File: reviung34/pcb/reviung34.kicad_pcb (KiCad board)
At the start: 2 copper layers, 214.3 x 107.1 mm, 95 parts, among them SW1 SW_PUSH, SW10 SW_PUSH, SW11 SW_PUSH, SW12 SW_PUSH, SW13 SW_PUSH, SW14 SW_PUSH, SW15 SW_PUSH, SW16 SW_PUSH, SW17 SW_PUSH, SW18 SW_PUSH, SW19 SW_PUSH, SW2 SW_PUSH, SW20 SW_PUSH, SW21 SW_PUSH, SW22 SW_PUSH, SW23 SW_PUSH, SW24 SW_PUSH, SW25 SW_PUSH, SW26 SW_PUSH, SW27 SW_PUSH, SW28 SW_PUSH, SW29 SW_PUSH, SW3 SW_PUSH, SW30 SW_PUSH, SW31 SW_PUSH, SW32 SW_PUSH, SW33 SW_PUSH, SW34 SW_PUSH, SW35 SW_PUSH, SW4 SW_PUSH, SW5 SW_PUSH, SW6 SW_PUSH, SW7 SW_PUSH, SW8 SW_PUSH, SW9 SW_PUSH, U1 ProMicro

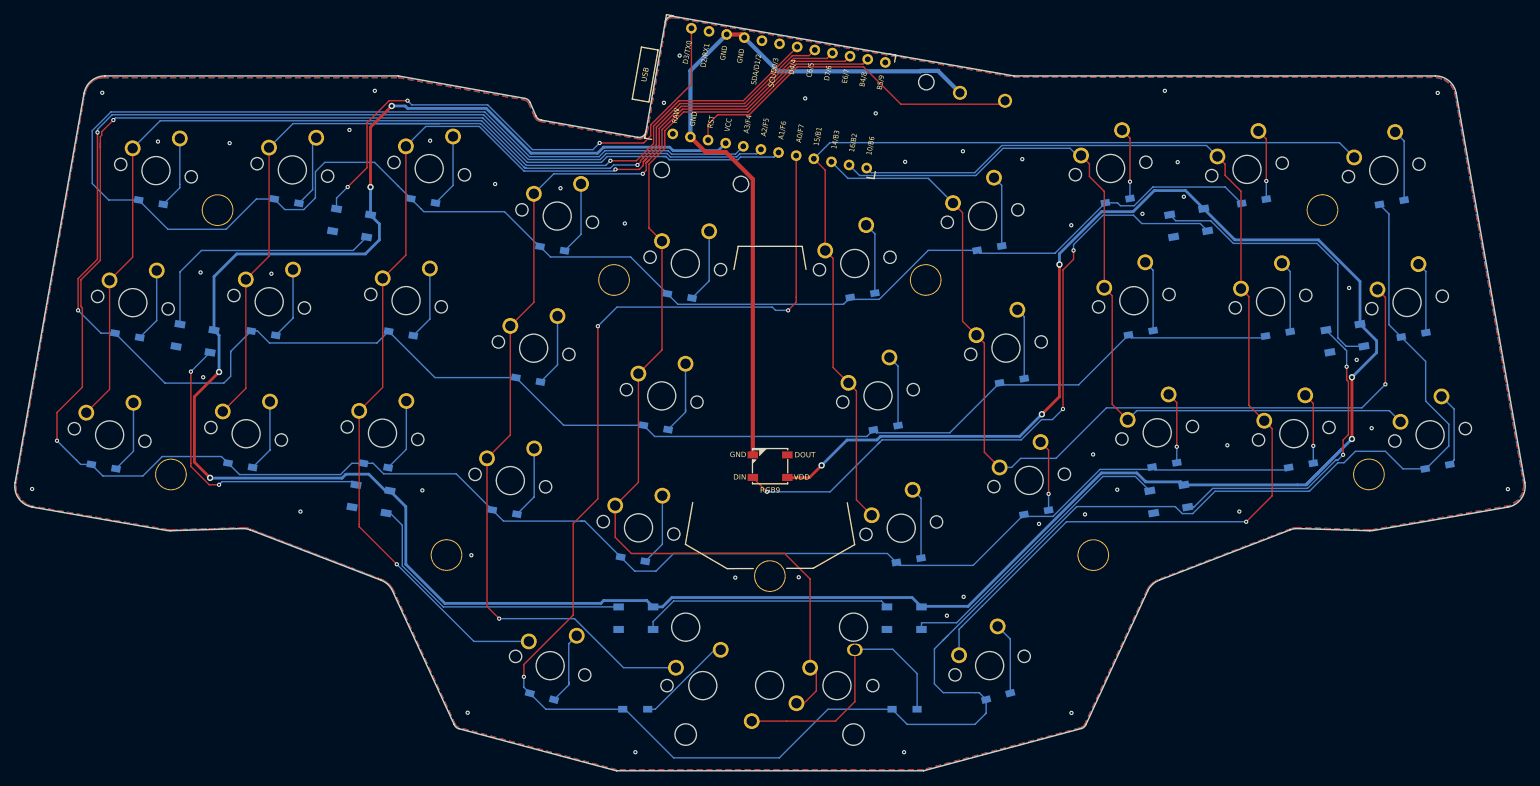
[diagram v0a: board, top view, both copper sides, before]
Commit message: choc version of r34
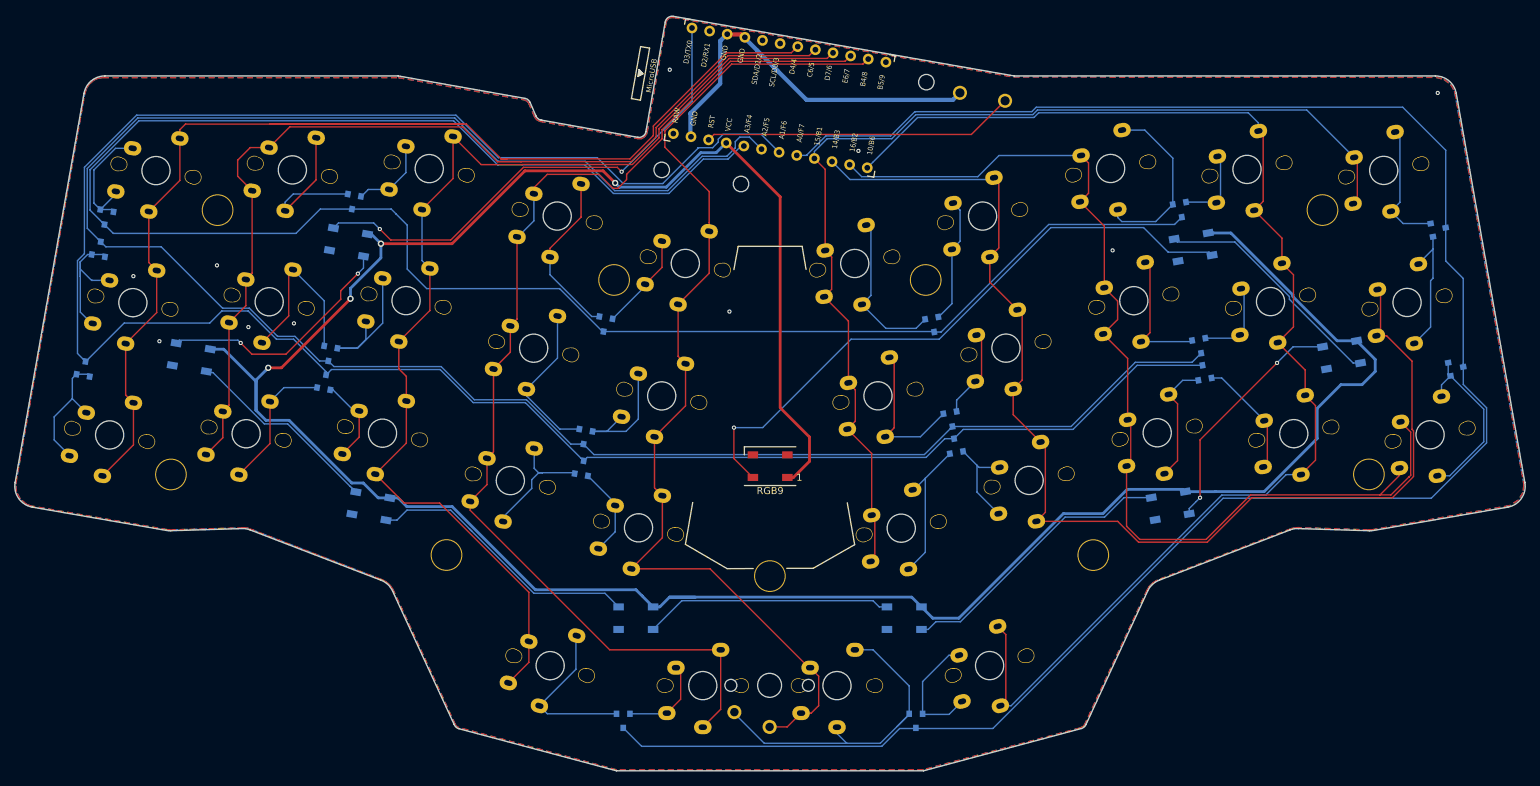
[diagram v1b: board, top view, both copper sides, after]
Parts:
- removed D12, D14, D17, D19, D2, D22, D23, D26, D27, D30, D32, D34, D4, D7, D9: 1N4148W, _reviung-kbd:D3_SMD_1side
- D1, D10, D11, D13, D15, D16, D18, D20, D21, D24, D25, D28, D29, D3, D31, D33, D5, D6, D8: value 1N4148W -> BAV70; footprint _reviung-kbd:D3_SMD_1side -> Package_TO_SOT_SMD:SOT-23
- RESET1: footprint _reviung-kbd:ResetSW_1side -> kbd-footprints:ResetSW_1side
- RGB1, RGB2, RGB3, RGB4, RGB5, RGB6, RGB7, RGB8, RGB9: footprint _reviung-kbd:LED_WS2812B_PLCC4_5.0x5.0mm_P3.2mm -> LED_SMD:LED_WS2812B_PLCC4_5.0x5.0mm_P3.2mm
- SW1, SW10, SW11, SW12, SW13, SW14, SW15, SW16, SW19, SW2, SW20, SW21, SW22, SW23, SW24, SW25, SW26, SW27, SW28, SW29, SW3, SW30, SW31, SW32, SW33, SW34, SW4, SW5, SW6, SW7, SW8, SW9: footprint _reviung-kbd:MXOnly-1U-NoLED -> kbd-footprints:CherryMX_Choc_1u
- SW17: footprint _reviung-kbd:MXOnly-1U-5pinRcut -> kbd-footprints:CherryMX_Choc_1u
- SW18: footprint _reviung-kbd:MXOnly-1U-5pinLcut -> kbd-footprints:CherryMX_Choc_1u
- SW35: footprint _reviung-kbd:MXOnly-2U-NoLED-or1Ux2 -> Keebio-Parts:Kailh-PG1350-1u-NoLED
- U1: footprint _reviung-kbd:ProMicro -> kbd-footprints:ProMicro_v3
- moved D28 14.9 mm to (164.2, 91.4), turned to 100 degrees
- moved D15 14.8 mm to (111.3, 94.6), turned to 80 degrees
- moved D29 14.3 mm to (199.5, 81.0), turned to 100 degrees
- moved D33 14.2 mm to (235.3, 80.4)
- moved D11 14.2 mm to (40.6, 80.5), turned to 80 degrees
- moved D13 13.9 mm to (74.8, 82.4), turned to 80 degrees
- moved D20 13.5 mm to (161.1, 74.3), turned to 280 degrees
- moved D6 12.9 mm to (42.8, 63.5), turned to 80 degrees
- moved D16 12.0 mm to (117.1, 130.5), turned to 270 degrees
- moved D5 11.4 mm to (114.5, 74.3), turned to 260 degrees
- moved D8 10.5 mm to (75.4, 78.5), turned to 260 degrees
- moved D24 10.2 mm to (163.6, 87.7), turned to 280 degrees
- moved D10 10.2 mm to (111.6, 90.2), turned to 260 degrees
- moved D3 9.93 mm to (78.8, 56.9), turned to 260 degrees
- moved D21 9.03 mm to (196.2, 58.0), turned to 280 degrees
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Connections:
- D1 pad 1: row0 -> Net-(D1-Pad1)
- D1 pad 2: Net-(D1-Pad2) -> Net-(D1-Pad1)
- D10 pad 1: row1 -> Net-(D10-Pad1)
- D11 pad 1: row2 -> Net-(D11-Pad1)
- D11 pad 2: Net-(D11-Pad2) -> Net-(D11-Pad1)
- D13 pad 1: row2 -> Net-(D13-Pad1)
- D15 pad 1: row2 -> Net-(D15-Pad1)
- D16 pad 1: row3 -> Net-(D16-Pad1)
- D18 pad 1: row3 -> Net-(D18-Pad1)
- D20 pad 1: row0 -> Net-(D20-Pad1)
- D21 pad 1: row0 -> Net-(D21-Pad1)
- D24 pad 1: row1 -> Net-(D24-Pad1)
- D25 pad 1: row1 -> Net-(D25-Pad1)
- D28 pad 1: row2 -> Net-(D28-Pad1)
- D29 pad 1: row2 -> Net-(D29-Pad1)
- D3 pad 1: row0 -> Net-(D3-Pad1)
- D31 pad 1: row3 -> Net-(D31-Pad1)
- D33 pad 1: row3 -> Net-(D33-Pad1)
- D33 pad 2: Net-(D33-Pad2) -> Net-(D33-Pad1)
- D5 pad 1: row0 -> Net-(D5-Pad1)
- D6 pad 1: row1 -> Net-(D6-Pad1)
- D6 pad 2: Net-(D6-Pad2) -> Net-(D6-Pad1)
- D8 pad 1: row1 -> Net-(D8-Pad1)
- SW1 pad 1: col0 -> Net-(D1-Pad1)
- SW1 pad 2: Net-(D1-Pad2) -> col0
- SW10 pad 1: col4 -> Net-(D10-Pad2)
- SW10 pad 2: Net-(D10-Pad2) -> col4
- SW11 pad 1: col0 -> Net-(D11-Pad1)
- SW11 pad 2: Net-(D11-Pad2) -> col0
- SW12 pad 2: Net-(D12-Pad2) -> Net-(D13-Pad2)
- SW13 pad 1: col2 -> Net-(D13-Pad1)
- SW13 pad 2: Net-(D13-Pad2) -> col2
- SW14 pad 2: Net-(D14-Pad2) -> Net-(D15-Pad2)
- SW15 pad 1: col4 -> Net-(D15-Pad1)
- SW15 pad 2: Net-(D15-Pad2) -> col4
- SW16 pad 2: Net-(D16-Pad2) -> Net-(D16-Pad1)
- SW17 pad 1: col3 -> Net-(D16-Pad2)
- SW17 pad 2: Net-(D17-Pad2) -> col3
- SW18 pad 2: Net-(D18-Pad2) -> Net-(D18-Pad1)
- SW19 pad 2: Net-(D19-Pad2) -> Net-(D20-Pad1)
- SW2 pad 2: Net-(D2-Pad2) -> Net-(D3-Pad1)
- SW20 pad 1: col6 -> Net-(D20-Pad2)
- SW20 pad 2: Net-(D20-Pad2) -> col6
- SW21 pad 2: Net-(D21-Pad2) -> Net-(D21-Pad1)
- SW22 pad 1: col8 -> Net-(D21-Pad2)
- SW22 pad 2: Net-(D22-Pad2) -> col8
- SW23 pad 2: Net-(D23-Pad2) -> Net-(D24-Pad1)
- SW24 pad 1: col6 -> Net-(D24-Pad2)
- SW24 pad 2: Net-(D24-Pad2) -> col6
- SW25 pad 2: Net-(D25-Pad2) -> Net-(D25-Pad1)
- SW26 pad 1: col8 -> Net-(D25-Pad2)
- SW26 pad 2: Net-(D26-Pad2) -> col8
- SW27 pad 2: Net-(D27-Pad2) -> Net-(D28-Pad2)
- SW28 pad 1: col6 -> Net-(D28-Pad1)
- SW28 pad 2: Net-(D28-Pad2) -> col6
- SW3 pad 1: col2 -> Net-(D3-Pad2)
- SW3 pad 2: Net-(D3-Pad2) -> col2
- SW30 pad 1: col8 -> Net-(D29-Pad1)
- SW30 pad 2: Net-(D30-Pad2) -> col8
- SW32 pad 2: Net-(D32-Pad2) -> Net-(D31-Pad1)
- SW33 pad 2: Net-(D33-Pad2) -> Net-(D33-Pad1)
- SW34 pad 1: col8 -> Net-(D18-Pad2)
- SW34 pad 2: Net-(D34-Pad2) -> col8
- SW35 pad 2: Net-(D18-Pad2) -> Net-(D18-Pad1)
- SW4 pad 2: Net-(D4-Pad2) -> Net-(D5-Pad1)
- SW5 pad 1: col4 -> Net-(D5-Pad2)
- SW5 pad 2: Net-(D5-Pad2) -> col4
- SW6 pad 1: col0 -> Net-(D6-Pad1)
- SW6 pad 2: Net-(D6-Pad2) -> col0
- SW7 pad 2: Net-(D7-Pad2) -> Net-(D8-Pad1)
- SW8 pad 1: col2 -> Net-(D8-Pad2)
- SW8 pad 2: Net-(D8-Pad2) -> col2
- SW9 pad 2: Net-(D9-Pad2) -> Net-(D10-Pad1)
- U1 pad 1: GND -> LED
- U1 pad 10: Net-(U1-Pad10) -> col3
- U1 pad 11: Net-(U1-Pad11) -> col4
- U1 pad 13: Net-(U1-Pad13) -> col8
- U1 pad 14: Net-(U1-Pad14) -> col7
- U1 pad 15: col8 -> col6
- U1 pad 16: col7 -> col5
- U1 pad 17: col6 -> row3
- U1 pad 18: col5 -> row2
- U1 pad 19: row3 -> row1
- U1 pad 2: GND -> Net-(U1-Pad2)
- U1 pad 20: row2 -> row0
- U1 pad 21: row1 -> VCC
- U1 pad 22: row0 -> reset
- U1 pad 23: VCC -> GND
- U1 pad 24: reset -> Net-(U1-Pad24)
- U1 pad 3: Net-(U1-Pad3) -> GND
- U1 pad 4: Net-(U1-Pad4) -> GND
- U1 pad 5: col0 -> Net-(U1-Pad5)
- U1 pad 6: col1 -> Net-(U1-Pad6)
- U1 pad 7: col2 -> col0
- U1 pad 8: col3 -> col1
- U1 pad 9: col4 -> col2
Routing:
- net VCC: track 464.4 -> 384.1 mm, vias 9 -> 4
- net GND: track 103.7 -> 55.1 mm, vias 47 -> 10
- net Net-(D18-Pad1): track 0.00 -> 47.7 mm
- net row3: track 322.8 -> 282.8 mm, vias 3 -> 0
- net col7: track 115.7 -> 151.3 mm
- net col0: track 147.2 -> 181.2 mm, vias 1 -> 0
- net col6: track 133.5 -> 167.2 mm, vias 1 -> 0
- net row2: track 342.4 -> 315.2 mm, vias 2 -> 0
- net Net-(D21-Pad1): track 0.00 -> 25.6 mm
- net Net-(D33-Pad1): track 0.00 -> 25.3 mm
- net col8: track 159.6 -> 184.7 mm, vias 1 -> 0
- net Net-(D8-Pad1): track 0.00 -> 24.9 mm
- net row1: track 317.7 -> 293.1 mm, vias 2 -> 0
- net Net-(D5-Pad1): track 0.00 -> 24.2 mm
- net Net-(D16-Pad1): track 0.00 -> 23.6 mm
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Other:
- board text added: "REVIUNG34 rev 1.0kb1 Designed by gtips 2021 choc by kbrock"
- board text removed: "REVIUNG34 rev 1.0 Designed by gtips 2021"
